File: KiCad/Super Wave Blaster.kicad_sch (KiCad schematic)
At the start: 16 parts, among them J1 EIAJ_Input, J2 PCM5102_I2S, J3 PCM5102_Audio, J4 Power Input, J5 Audio_Out, J6 Power Input, U1 TLV73333PDBV, U2 CD74HCT14PWR, U3 SN74HC595PWR, U4 SN74LVC8T245PWR

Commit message: Revision v1.1
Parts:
- added C5, C8: 1uf, Capacitor_SMD:C_0805_2012Metric, symbol Device:C_Polarized
- added J7: Audio Out, Connector_PinHeader_2.54mm:PinHeader_1x02_P2.54mm_Horizontal, symbol Connector:Conn_01x02_Pin
- added R1, R2: 24k, Resistor_SMD:R_0805_2012Metric, symbol Device:R
- J5: value Audio_Out -> Audio_Jack
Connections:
- net AUDIO_L: now also C5.1
- net AUDIO_R: now also C8.1
- new net: C8.2, R2.1
- new net: C5.2, R1.1
- new net: J7.2 (Pin_2), R1.2
- new net: J7.1 (Pin_1), R2.2

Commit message: Cleanup schematic layout
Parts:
- C1, C2: symbol Device:C -> Device:C_Polarized
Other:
- moved on the sheet: C3, C4, C5, C6, C7, C8, J1, J2, J3, J4, J5, J6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

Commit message: V1.4
Adjust J7 opamp outputs, cleaned up ground plane, changed all 0805 pads to hand solder sizing.
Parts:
- C1, C2, C3, C4, C5, C6, C7, C8: footprint Capacitor_SMD:C_0805_2012Metric -> Capacitor_SMD:C_0805_2012Metric_Pad1.18x1.45mm_HandSolder
- J7: footprint Connector_PinHeader_2.54mm:PinHeader_1x02_P2.54mm_Horizontal -> Connector_PinHeader_2.54mm:PinHeader_1x02_P2.54mm_Vertical
- R1, R2: footprint Resistor_SMD:R_0805_2012Metric -> Resistor_SMD:R_0805_2012Metric_Pad1.20x1.40mm_HandSolder
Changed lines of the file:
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@@
 			)
 		)
-		(property "Footprint" "Capacitor_SMD:C_0805_2012Metric"
+		(property "Footprint" "Capacitor_SMD:C_0805_2012Metric_Pad1.18x1.45mm_HandSolder"
 			(at 54.61 120.3452 0)
 			(effects
@@
 			)
 		)
-		(property "Footprint" "Resistor_SMD:R_0805_2012Metric"
+		(property "Footprint" "Resistor_SMD:R_0805_2012Metric_Pad1.20x1.40mm_HandSolder"
 			(at 50.8 129.032 90)
 			(effects
@@
 			)
 		)
-		(property "Footprint" "Capacitor_SMD:C_0805_2012Metric"
+		(property "Footprint" "Capacitor_SMD:C_0805_2012Metric_Pad1.18x1.45mm_HandSolder"
 			(at 54.61 131.7752 0)
 			(effects
@@
 			)
 		)
-		(property "Footprint" "Capacitor_SMD:C_0805_2012Metric"
+		(property "Footprint" "Capacitor_SMD:C_0805_2012Metric_Pad1.18x1.45mm_HandSolder"
 			(at 100.0252 72.39 0)
 			(effects
@@
 			)
 		)
-		(property "Footprint" "Capacitor_SMD:C_0805_2012Metric"
+		(property "Footprint" "Capacitor_SMD:C_0805_2012Metric_Pad1.18x1.45mm_HandSolder"
 			(at 99.06 100.0252 0)
 			(effects
@@
 			)
 		)
-		(property "Footprint" "Capacitor_SMD:C_0805_2012Metric"
+		(property "Footprint" "Capacitor_SMD:C_0805_2012Metric_Pad1.18x1.45mm_HandSolder"
 			(at 121.92 98.0948 0)
 			(effects
@@
 			)
 		)
-		(property "Footprint" "Capacitor_SMD:C_0805_2012Metric"
+		(property "Footprint" "Capacitor_SMD:C_0805_2012Metric_Pad1.18x1.45mm_HandSolder"
 			(at 195.8848 59.69 0)
 			(effects
@@
 			)
 		)
-		(property "Footprint" "Capacitor_SMD:C_0805_2012Metric"
+		(property "Footprint" "Capacitor_SMD:C_0805_2012Metric_Pad1.18x1.45mm_HandSolder"
 			(at 125.4252 72.39 0)
 			(effects
@@
 			)
 		)
-		(property "Footprint" "Resistor_SMD:R_0805_2012Metric"
+		(property "Footprint" "Resistor_SMD:R_0805_2012Metric_Pad1.20x1.40mm_HandSolder"
 			(at 50.8 117.602 90)
 			(effects
@@
 			)
 		)
-		(property "Footprint" "Capacitor_SMD:C_0805_2012Metric"
+		(property "Footprint" "Capacitor_SMD:C_0805_2012Metric_Pad1.18x1.45mm_HandSolder"
 			(at 191.77 127.3048 0)
 			(effects
@@
 			)
 		)
-		(property "Footprint" "Connector_PinHeader_2.54mm:PinHeader_1x02_P2.54mm_Horizontal"
+		(property "Footprint" "Connector_PinHeader_2.54mm:PinHeader_1x02_P2.54mm_Vertical"
 			(at 38.1 124.46 0)
 			(effects

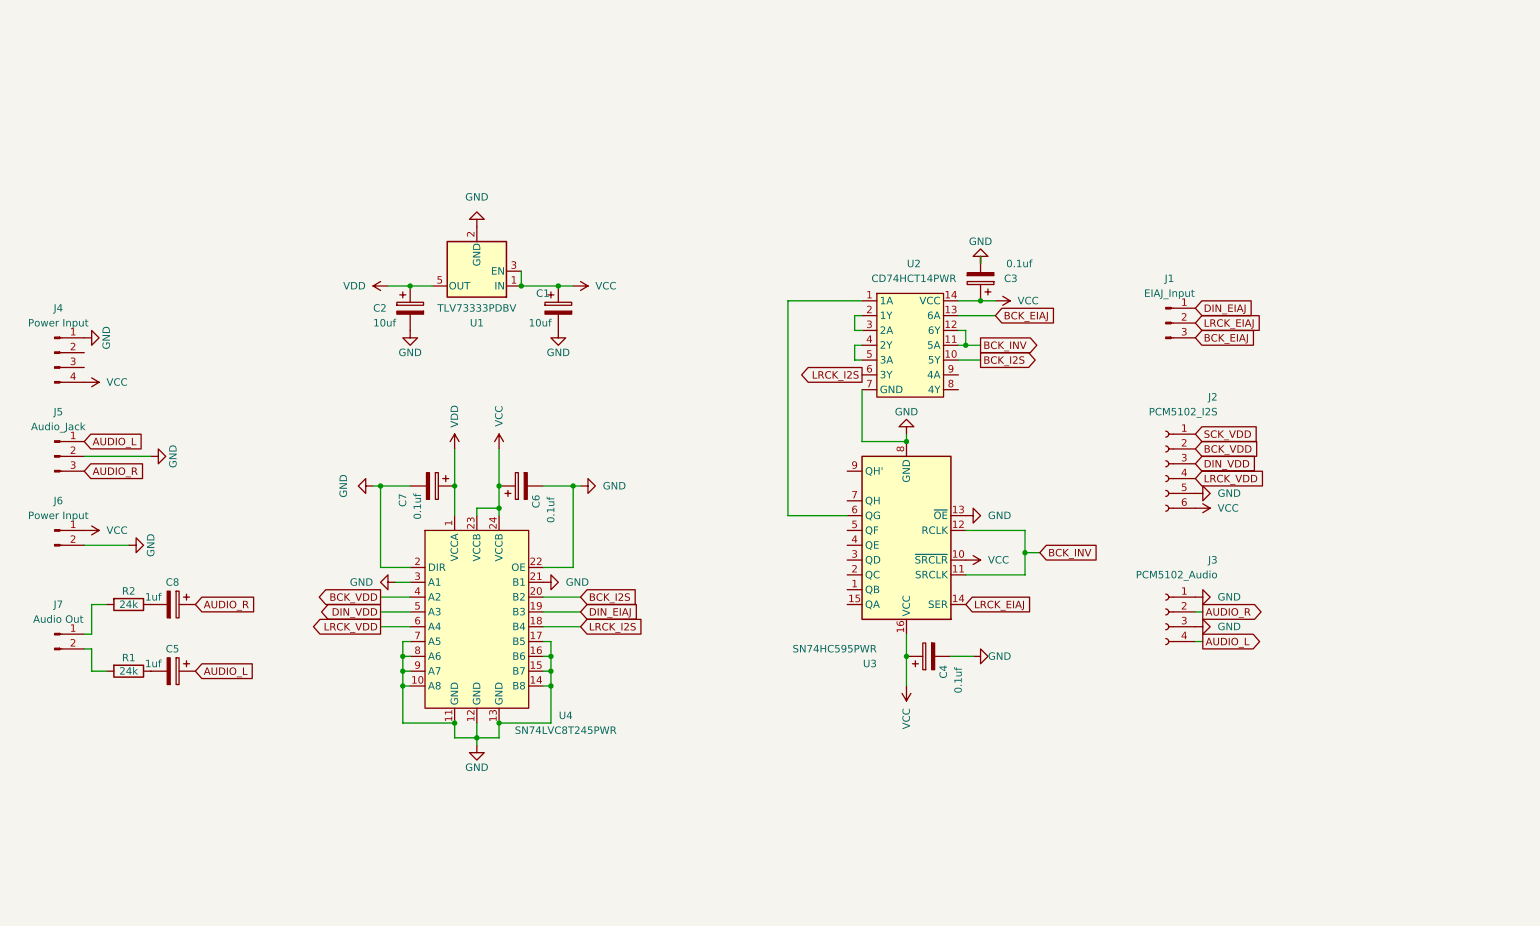
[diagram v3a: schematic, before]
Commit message: V1.5
Refactored for underside mounting only and optional expansion for S/PDIF output. Full PCM5102A integration. Optimized audio quality.
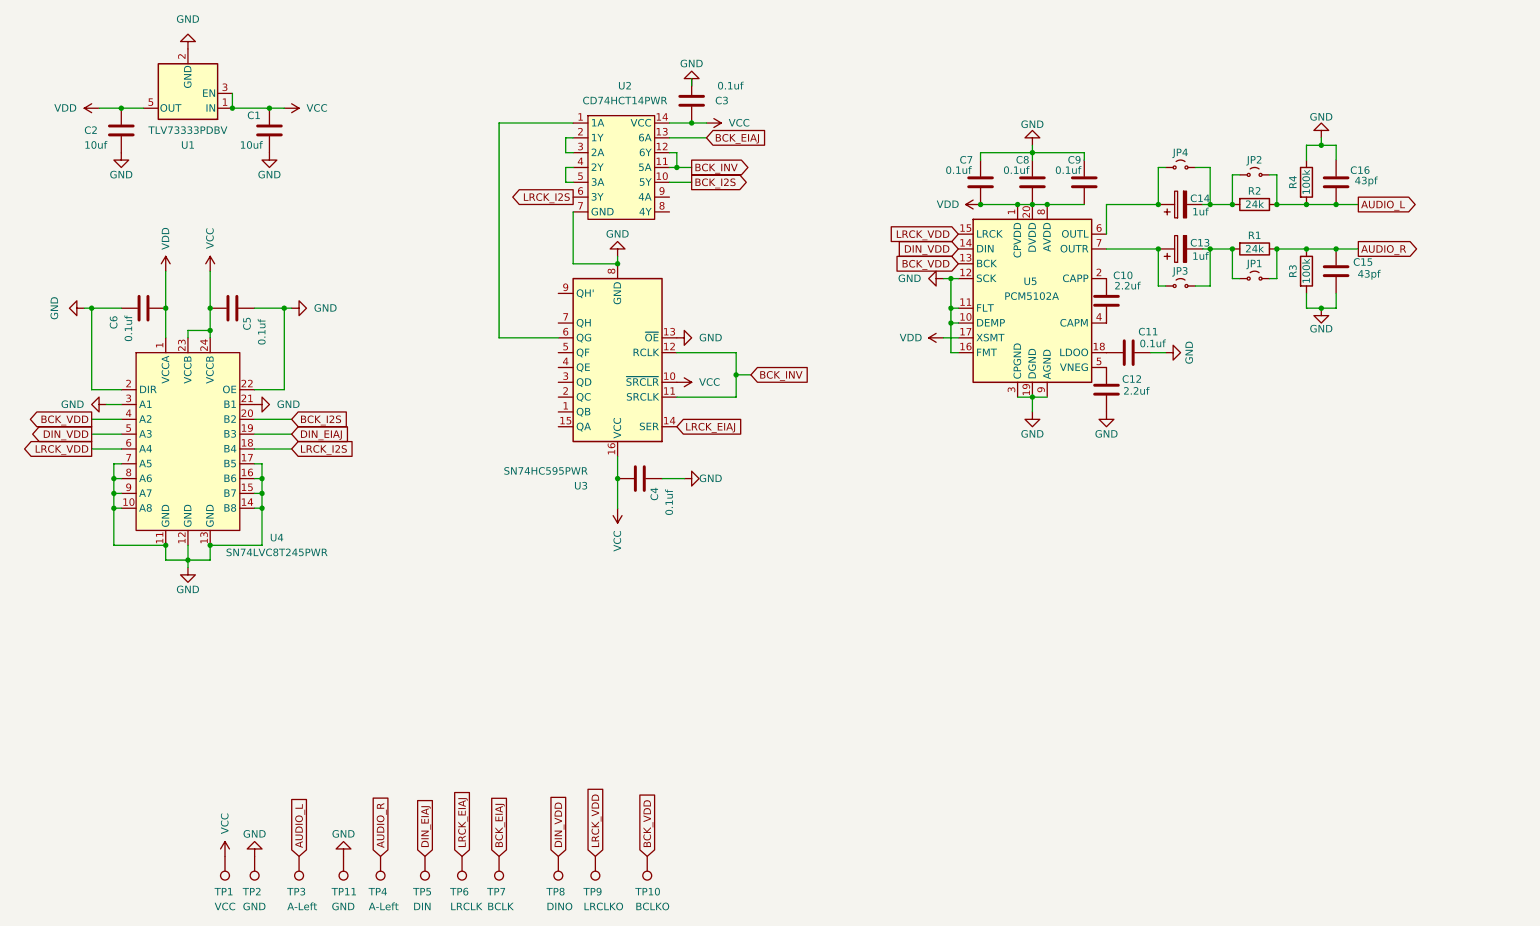
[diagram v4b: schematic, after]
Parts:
- removed J1: EIAJ_Input, Connector_PinHeader_2.54mm:PinHeader_1x03_P2.54mm_Horizontal, symbol Connector:Conn_01x03_Pin
- removed J2: PCM5102_I2S, Connector_PinSocket_2.54mm:PinSocket_1x06_P2.54mm_Vertical, symbol Connector:Conn_01x06_Socket
- removed J3: PCM5102_Audio, Connector_PinSocket_2.54mm:PinSocket_1x04_P2.54mm_Vertical, symbol Connector:Conn_01x04_Socket
- removed J4: Power Input, Connector_PinHeader_2.54mm:PinHeader_1x04_P2.54mm_Vertical, symbol Connector:Conn_01x04_Pin
- removed J5: Audio_Jack, Connector_PinHeader_2.54mm:PinHeader_1x03_P2.54mm_Horizontal, symbol Connector:Conn_01x03_Pin
- removed J6: Power Input, Connector_PinHeader_2.54mm:PinHeader_1x02_P2.54mm_Horizontal, symbol Connector:Conn_01x02_Pin
- removed J7: Audio Out, Connector_PinHeader_2.54mm:PinHeader_1x02_P2.54mm_Vertical, symbol Connector:Conn_01x02_Pin
- added C10, C12: 2.2uf, Capacitor_SMD:C_0805_2012Metric_Pad1.18x1.45mm_HandSolder, symbol Device:C
- added C11, C7, C8, C9: 0.1uf, Capacitor_SMD:C_0805_2012Metric_Pad1.18x1.45mm_HandSolder, symbol Device:C
- added C15, C16: 43pf, Capacitor_SMD:C_0805_2012Metric_Pad1.18x1.45mm_HandSolder, symbol Device:C
- added JP1, JP2, JP3, JP4: ~, Jumper:SolderJumper-2_P1.3mm_Open_RoundedPad1.0x1.5mm, symbol Jumper:Jumper_2_Small_Open
- added R1, R2: 24k, Resistor_SMD:R_0805_2012Metric_Pad1.20x1.40mm_HandSolder, symbol Device:R
- added TP1: VCC, TestPoint:TestPoint_Pad_1.5x1.5mm, symbol Connector:TestPoint
- added TP10: BCLKO, TestPoint:TestPoint_Pad_1.5x1.5mm, symbol Connector:TestPoint
- added TP11, TP2: GND, TestPoint:TestPoint_Pad_1.5x1.5mm, symbol Connector:TestPoint
- added TP3, TP4: A-Left, TestPoint:TestPoint_Pad_1.5x1.5mm, symbol Connector:TestPoint
- added TP5: DIN, TestPoint:TestPoint_Pad_1.5x1.5mm, symbol Connector:TestPoint
- added TP6: LRCLK, TestPoint:TestPoint_Pad_1.5x1.5mm, symbol Connector:TestPoint
- added TP7: BCLK, TestPoint:TestPoint_Pad_1.5x1.5mm, symbol Connector:TestPoint
- added TP8: DINO, TestPoint:TestPoint_Pad_1.5x1.5mm, symbol Connector:TestPoint
- added TP9: LRCLKO, TestPoint:TestPoint_Pad_1.5x1.5mm, symbol Connector:TestPoint
- added U5: PCM5102A, Package_SO:TSSOP-20_4.4x6.5mm_P0.65mm, symbol Audio:PCM5100
- C1, C2, C3, C4: symbol Device:C_Polarized -> Device:C
- C13: renamed from C8; footprint Capacitor_SMD:C_0805_2012Metric_Pad1.18x1.45mm_HandSolder -> Capacitor_SMD:C_Elec_6.3x5.8
- C14: renamed from C5; footprint Capacitor_SMD:C_0805_2012Metric_Pad1.18x1.45mm_HandSolder -> Capacitor_SMD:C_Elec_6.3x5.8
- C5: renamed from C6; symbol Device:C_Polarized -> Device:C
- C6: renamed from C7; symbol Device:C_Polarized -> Device:C
- R3: renamed from R2; value 24k -> 100k
- R4: renamed from R1; value 24k -> 100k
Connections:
- net AUDIO_L: now also R4.2, C16.1, JP2.2 (B), R2.1, TP3.1; no longer C14.1
- net AUDIO_R: now also R3.1, C15.2, JP1.2 (B), R1.1, TP4.1; no longer C13.1
- net BCK_EIAJ: now also TP7.1
- net BCK_VDD: now also TP10.1, U5.13 (BCK)
- net DIN_EIAJ: now also TP5.1
- net DIN_VDD: now also TP8.1, U5.14 (DIN)
- net GND: now also R3.2, R4.1, C11.2, C12.1, C15.1, C16.2, C7.2, C8.2, C9.2, TP11.1, TP2.1, U5.10 (DEMP), U5.11 (FLT), U5.12 (SCK), U5.16 (FMT), U5.19 (DGND), U5.3 (CPGND), U5.9 (AGND)
- net LRCK_EIAJ: now also TP6.1
- net LRCK_VDD: now also TP9.1, U5.15 (LRCK)
- net VCC: now also TP1.1
- net VDD: now also C7.1, C8.1, C9.1, U5.1 (CPVDD), U5.17 (XSMT), U5.20 (DVDD), U5.8 (AVDD)
- net at C13.2: now also JP1.1 (A), JP3.2 (B), R1.2; no longer R3.1
- net at C14.2: now also JP2.1 (A), JP4.2 (B), R2.2; no longer R4.1
- new net: C13.1, JP3.1 (A), U5.7 (OUTR)
- new net: C12.2, U5.5 (VNEG)
- new net: C14.1, JP4.1 (A), U5.6 (OUTL)
- new net: C11.1, U5.18 (LDOO)
- new net: C10.2, U5.2 (CAPP)
- new net: C10.1, U5.4 (CAPM)
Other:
- moved on the sheet: C13, C14, R3, R4, U1, U2, U3, U4

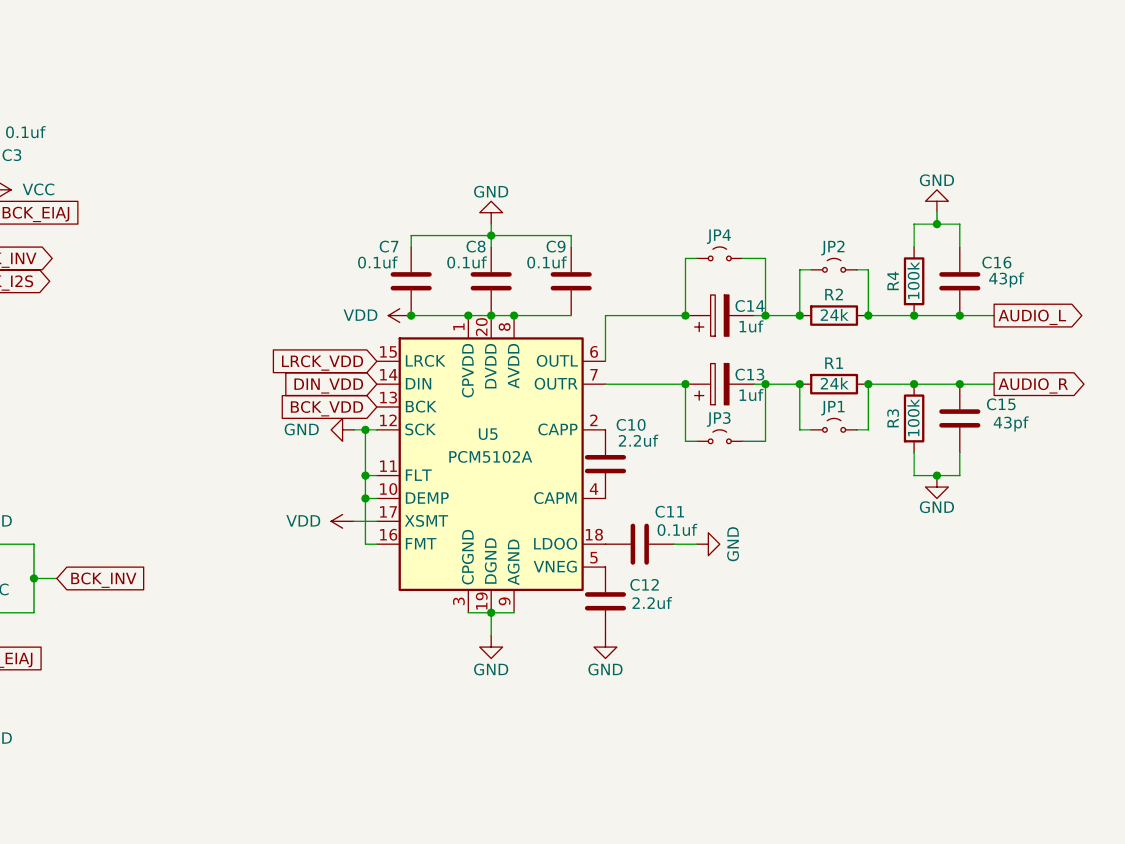
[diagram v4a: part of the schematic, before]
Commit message: V1.6
Refactor analog circuit with 0.1uf coupling and 100k pull down.
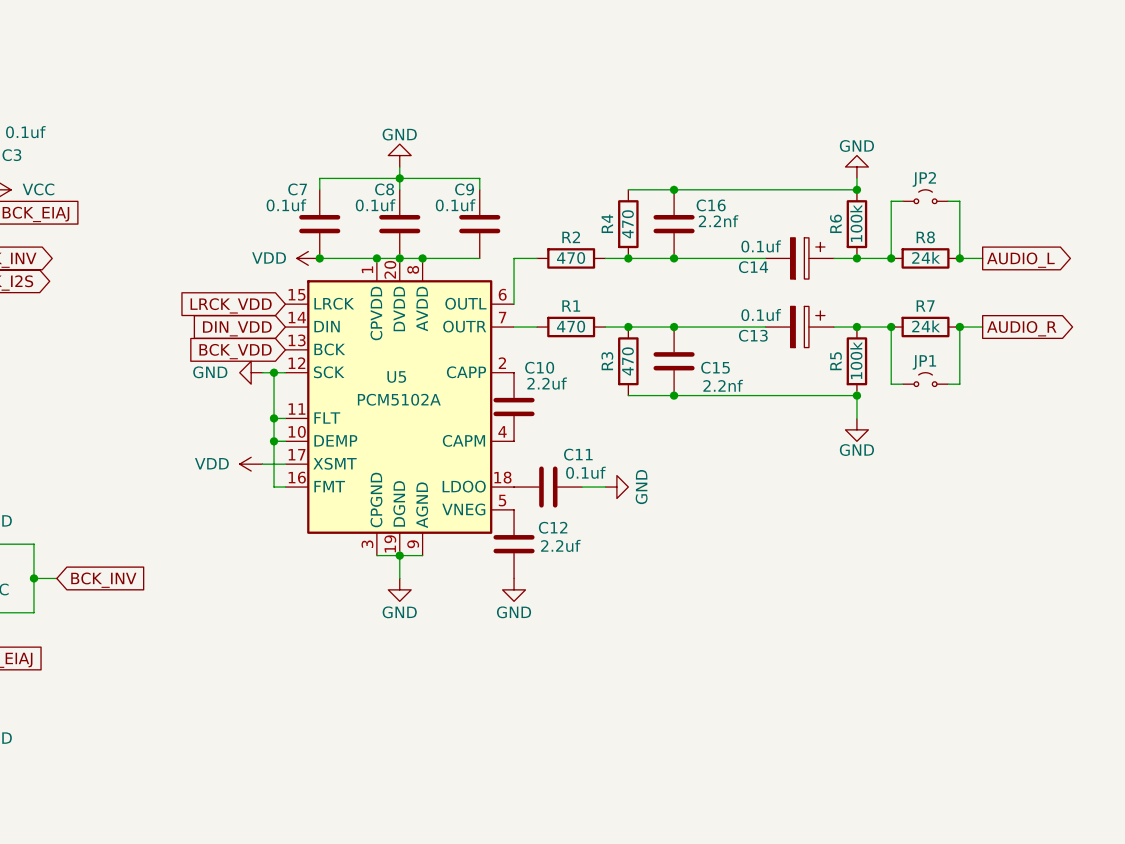
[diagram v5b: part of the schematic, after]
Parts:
- removed JP3, JP4: ~, Jumper:SolderJumper-2_P1.3mm_Open_RoundedPad1.0x1.5mm, symbol Jumper:Jumper_2_Small_Open
- added R1, R2, R3, R4: 470, Resistor_SMD:R_0805_2012Metric_Pad1.20x1.40mm_HandSolder, symbol Device:R
- C13, C14: value 1uf -> 0.1uf; footprint Capacitor_SMD:C_Elec_6.3x5.8 -> Capacitor_SMD:C_1206_3216Metric_Pad1.33x1.80mm_HandSolder
- C15, C16: value 43pf -> 2.2nf
- renumbered R3 to R5, R4 to R6, R1 to R7, R2 to R8
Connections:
- net AUDIO_L: no longer C16.1, R6.2
- net AUDIO_R: no longer C15.2, R5.1
- net GND: now also R3.2, R4.1
- net at C13.1: now also JP1.1 (A), R5.1, R7.2; no longer U5.7 (OUTR)
- net at U5.6 (OUTL): now also R2.2; no longer C14.1
- net at JP2.1 (A), R8.2: now also C14.1, R6.2; no longer C14.2
- new net: C13.2, C15.2, R1.1, R3.1
- new net: C14.2, C16.1, R2.1, R4.2
- new net: R1.2, U5.7 (OUTR)
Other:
- moved on the sheet: C10, C11, C12, C13, C14, C15, C16, C7, C8, C9, R5, R6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

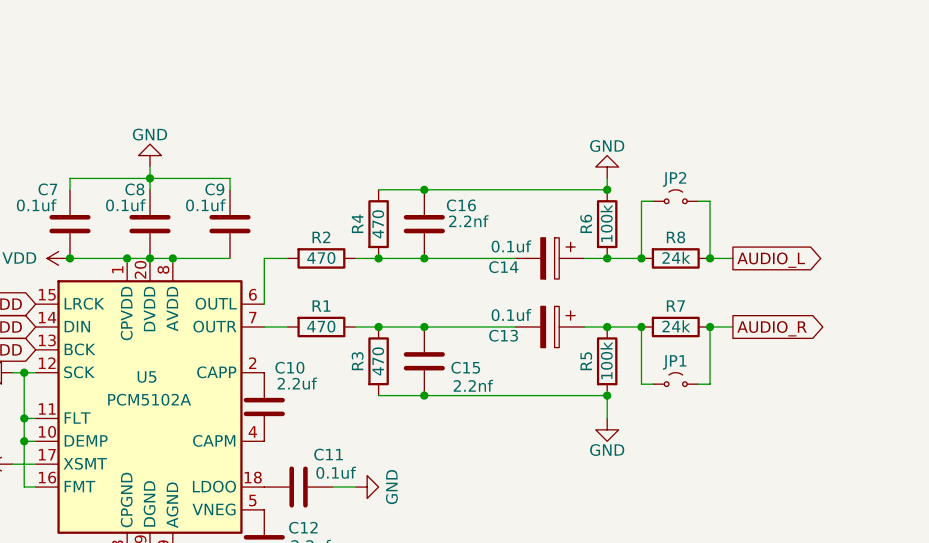
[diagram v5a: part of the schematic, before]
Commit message: Change S-Mix values, jumper notes
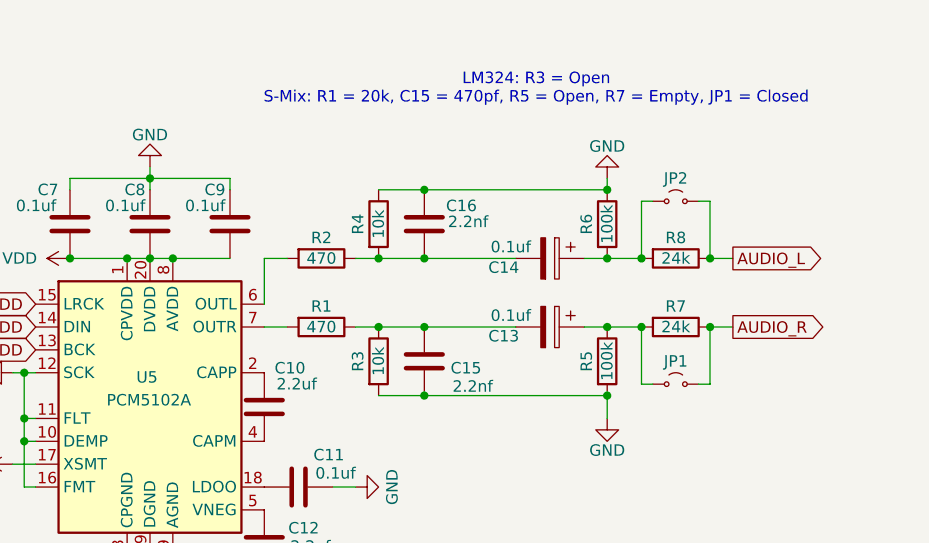
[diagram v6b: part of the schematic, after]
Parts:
- R3, R4: value 470 -> 10k
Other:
- note added: "LM324: R3 = Open S-Mix: R1 = 20k, C15 = 470pf, R5 = Open, R7 = Empty, JP1 = Closed"
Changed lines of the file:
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@@
 		)
 	)
+	(text "LM324: R3 = Open\nS-Mix: R1 = 20k, C15 = 470pf, R5 = Open, R7 = Empty, JP1 = Closed"
+		(exclude_from_sim no)
+		(at 238.506 25.654 0)
+		(effects
+			(font
+				(size 1.27 1.27)
+			)
+		)
+	)
 	(global_label "BCK_VDD"
 		(shape input)
@@
 			)
 		)
-		(property "Value" "470"
+		(property "Value" "10k"
 			(at 220.98 55.88 90)
 			(effects
@@
 			)
 		)
-		(property "Value" "470"
+		(property "Value" "10k"
 			(at 220.98 40.64 90)
 			(effects
